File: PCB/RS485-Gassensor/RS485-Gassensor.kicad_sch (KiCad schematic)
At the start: 22 parts, among them J1 Conn_01x04, J2 Conn_01x04, U1 STM8S003F3P, U2 MICS-8614, U3 R-785.0-1.0, U4 LT1785xS8, U5 OP179GRT

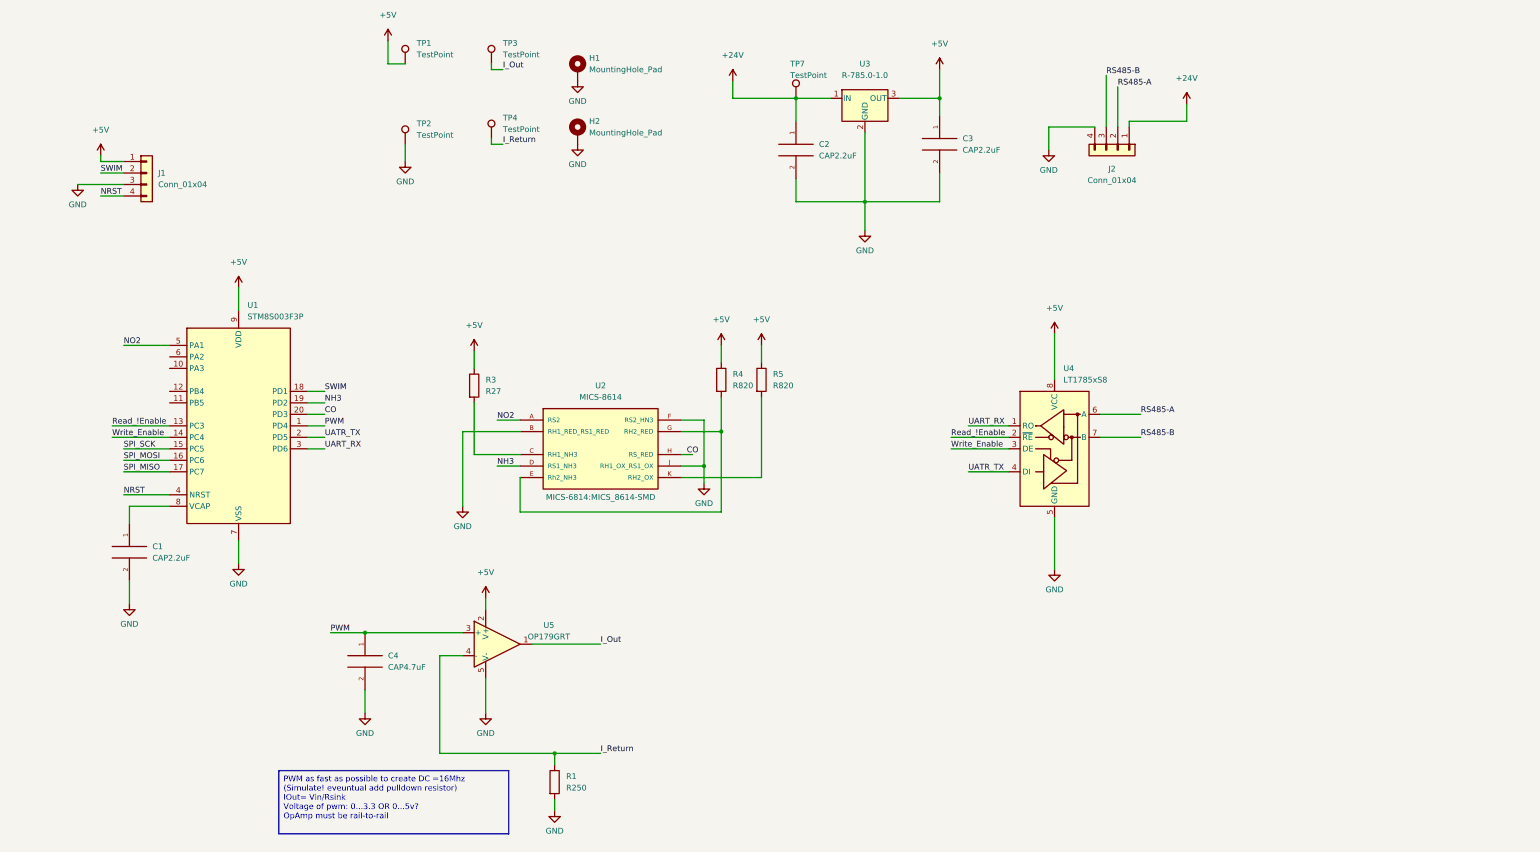
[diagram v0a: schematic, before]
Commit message: clean up, minor extension
cleaned up /reorganized scematic,
added optional termination resistor for RS-485
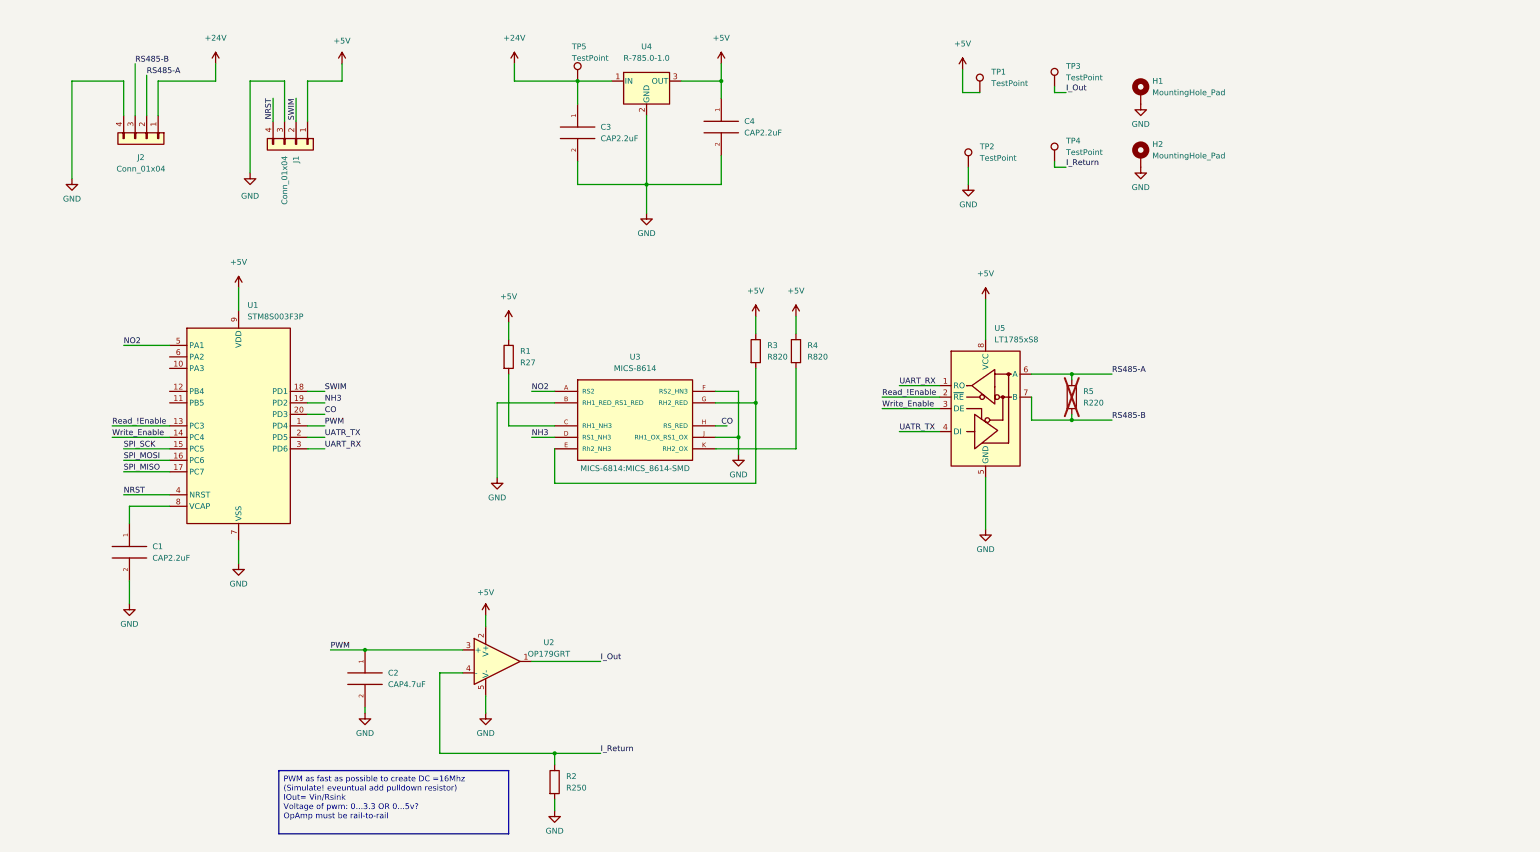
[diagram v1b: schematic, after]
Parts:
- added R5: R220, Capacitor_SMD:C_0603_1608Metric, symbol Device:R
- renumbered C4 to C2, C2 to C3, C3 to C4, R3 to R1, R1 to R2, R4 to R3, R5 to R4, TP7 to TP5, U5 to U2, U2 to U3, U3 to U4, U4 to U5
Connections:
- net RS485-A: now also R5.1
- net RS485-B: now also R5.2
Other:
- moved on the sheet: C2, C3, C4, H1, H2, J1, J2, R1, R3, R4, TP1, TP2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

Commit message: restarted Project.
new PCB, improved component chioce
strarted program with STM32 IDE
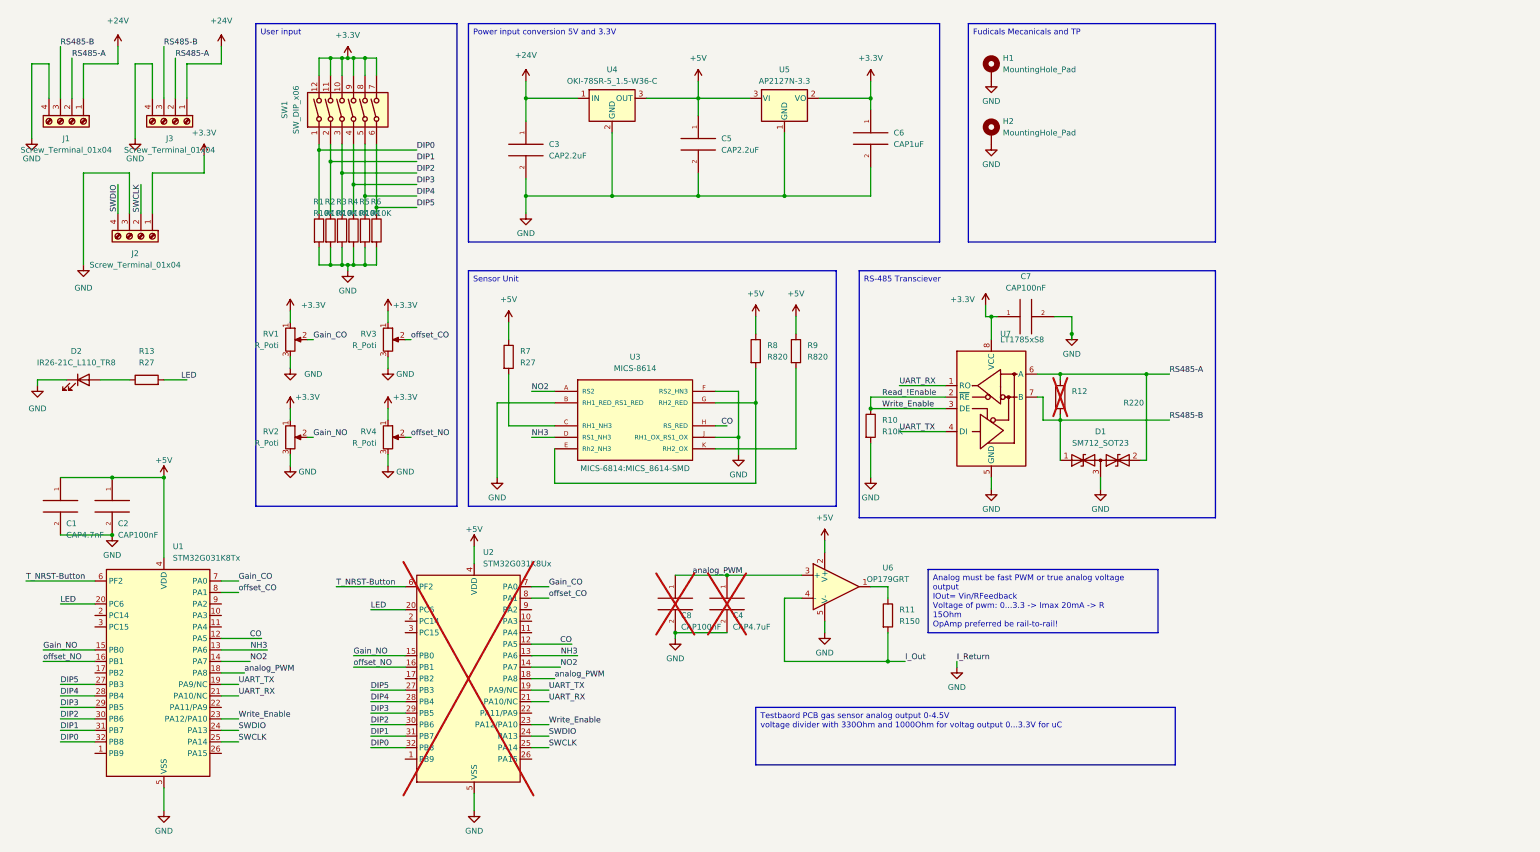
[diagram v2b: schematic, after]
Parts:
- removed J1: Conn_01x04, Connector_PinHeader_2.54mm:PinHeader_1x04_P2.54mm_Vertical, symbol Connector_Generic:Conn_01x04
- removed J2: Conn_01x04, Connector_Phoenix_SPT:PhoenixContact_SPT_1.5_4-H-3.5_1x04_P3.5mm_Horizontal, symbol Connector_Generic:Conn_01x04
- removed TP1, TP2, TP3, TP4, TP5: TestPoint, TestPoint:TestPoint_Pad_D1.0mm, symbol Connector:TestPoint
- removed U1: STM8S003F3P, Package_SO:TSSOP-20_4.4x6.5mm_P0.65mm, symbol MCU_ST_STM8:STM8S003F3P
- removed U4: R-785.0-1.0, Converter_DCDC:Converter_DCDC_RECOM_R-78E-0.5_THT, symbol Regulator_Switching:R-785.0-1.0
- added C2, C7, C8: CAP100nF, Capacitor_SMD:C_0603_1608Metric, symbol pspice:CAP
- added C6: CAP1uF, Capacitor_SMD:C_0603_1608Metric, symbol pspice:CAP
- added D1: SM712_SOT23, Package_TO_SOT_SMD:SOT-23, symbol Diode:SM712_SOT23
- added D2: IR26-21C_L110_TR8, LED_SMD:LED_1206_3216Metric, symbol LED:IR26-21C_L110_TR8
- added J1, J3: Screw_Terminal_01x04, Connector_Phoenix_SPT:PhoenixContact_SPT_1.5_4-H-3.5_1x04_P3.5mm_Horizontal, symbol Connector:Screw_Terminal_01x04
- added J2: Screw_Terminal_01x04, Connector_PinHeader_2.54mm:PinHeader_1x04_P2.54mm_Vertical, symbol Connector:Screw_Terminal_01x04
- added R1, R10, R3, R4, R5, R6: R10K, Capacitor_SMD:C_0603_1608Metric, symbol Device:R
- added R11: R150, Capacitor_SMD:C_1206_3216Metric, symbol Device:R
- added R13: R27, Capacitor_SMD:C_0603_1608Metric, symbol Device:R
- added RV1, RV2, RV3, RV4: R_Poti, PCM_Potentiometer_SMD_AKL:Potentiometer_ACP_CA6-VSMD_Vertical, symbol Device:R_Potentiometer
- added SW1: SW_DIP_x06, Package_DIP:SMDIP-12_W9.53mm, symbol Switch:SW_DIP_x06
- added U1: STM32G031K8Tx, Package_QFP:LQFP-32_7x7mm_P0.8mm, symbol MCU_ST_STM32G0:STM32G031K8Tx
- added U2: STM32G031K8Ux, Package_DFN_QFN:QFN-32-1EP_5x5mm_P0.5mm_EP3.45x3.45mm, symbol MCU_ST_STM32G0:STM32G031K8Ux
- added U4: OKI-78SR-5_1.5-W36-C, Converter_DCDC:Converter_DCDC_Murata_OKI-78SR_Vertical, symbol Converter_DCDC:OKI-78SR-5_1.5-W36-C
- added U5: AP2127N-3.3, Package_TO_SOT_SMD:SOT-23, symbol Regulator_Linear:AP2127N-3.3
- C1: value CAP2.2uF -> CAP4.7nF
- C4: renamed from C2; now not fitted; now left out of the parts list
- R2: value R250 -> R10K
- renumbered C4 to C5, R5 to R12, R1 to R7, R3 to R8, R4 to R9, U2 to U6, U5 to U7
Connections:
- net Write_Enable is gone; now on net Read_!Enable: U7.3 (DE)
- net +24V: now also J1.1 (Pin_1), J3.1 (Pin_1), U4.1 (IN)
- net +5V: now also C1.1, C2.1, U1.4 (VDD), U2.4 (VDD), U4.3 (OUT), U5.3 (VI); no longer U7.8 (VCC)
- net CO: now also U1.12 (PA5), U2.12 (PA5)
- net GND: now also C2.2, C6.2, C7.2, C8.2, D1.3 (common), D2.1 (K), J1.4 (Pin_4), J2.3 (Pin_3), J3.4 (Pin_4), R1.2, R10.2, R3.2, R4.2, R5.2, R6.2, RV1.3, RV2.3, RV3.3, RV4.3, U1.5 (VSS), U2.33 (VSS), U2.5 (VSS), U4.2 (GND), U5.1 (GND)
- net I_Out: now also U6.4 (-), R11.2; no longer U6.1
- net NH3: now also U1.13 (PA6), U2.13 (PA6)
- net NO2: now also U1.14 (PA7), U2.14 (PA7)
- net RS485-A: now also D1.2 (A2), J1.2 (Pin_2), J3.2 (Pin_2)
- net RS485-B: now also D1.1 (A1), J1.3 (Pin_3), J3.3 (Pin_3)
- net Read_!Enable: now also R10.1, U1.23 (PA12/PA10), U2.23 (PA12/PA10)
- net UART_RX: now also U1.21 (PA10/NC), U2.21 (PA10/NC)
- net I_Return renamed DIP1
- net DIP1: now also SW1.2, U1.31 (PB7), U2.31 (PB7); no longer U6.4 (-)
- net PWM renamed analog_PWM
- net analog_PWM: now also C8.1, U1.18 (PA8), U2.18 (PA8)
- net UATR_TX renamed UART_TX
- net UART_TX: now also U1.19 (PA9/NC), U2.19 (PA9/NC)
- new net: R11.1, U6.1
- new net: D2.2 (A), R13.1
- new net +3.3V: C6.1, C7.1, J2.1 (Pin_1), RV1.1, RV2.1, RV3.1, RV4.1, SW1.10, SW1.11, SW1.12, SW1.7, SW1.8, SW1.9, U5.2 (VO), U7.8 (VCC)
- new net DIP0: R1.1, SW1.1, U1.32 (PB8), U2.32 (PB8)
- new net DIP2: R3.1, SW1.3, U1.30 (PB6), U2.30 (PB6)
- new net DIP3: R4.1, SW1.4, U1.29 (PB5), U2.29 (PB5)
- new net DIP4: R5.1, SW1.5, U1.28 (PB4), U2.28 (PB4)
- new net DIP5: R6.1, SW1.6, U1.27 (PB3), U2.27 (PB3)
- new net Gain_CO: RV1.2, U1.7 (PA0), U2.7 (PA0)
- new net Gain_NO: RV2.2, U1.15 (PB0), U2.15 (PB0)
- new net LED: R13.2, U1.20 (PC6), U2.20 (PC6)
- new net SWCLK: J2.2 (Pin_2), U1.25 (PA14), U2.25 (PA14)
- new net SWDIO: J2.4 (Pin_4), U1.24 (PA13), U2.24 (PA13)
- new net T_NRST-Button: U1.6 (PF2), U2.6 (PF2)
- new net offset_CO: RV3.2, U1.8 (PA1), U2.8 (PA1)
- new net offset_NO: RV4.2, U1.16 (PB1), U2.16 (PB1)
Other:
- moved on the sheet: C3, C5, H1, H2, R12, U6, U7

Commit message: new PCB
new PCB, working DMA
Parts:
- removed J3: Screw_Terminal_01x04, Connector_Phoenix_SPT:PhoenixContact_SPT_1.5_4-H-3.5_1x04_P3.5mm_Horizontal, symbol Connector:Screw_Terminal_01x04
- removed U3: MICS-8614, MICS-6814:MICS_8614-SMD, symbol MICS-8614:MICS-8614
- removed U6: OP179GRT, PCM_Package_TO_SOT_SMD_AKL:SOT-23-5, symbol Amplifier_Operational:OP179GRT
- added FD1, FD2: ~, Custom_Library:Alignement_Testpoint_2Layer, symbol Custom:Alignement_Testpoint
- added H3, H4: MountingHole_Pad, MountingHole:MountingHole_3.2mm_M3_DIN965_Pad, symbol Mechanical:MountingHole_Pad
- added J1: Screw_Terminal_01x08, Connector_Phoenix_SPT:1862068, symbol Connector:Screw_Terminal_01x08
- added J4, J5: Screw_Terminal_01x06, Connector_Phoenix_SPT:1071000, symbol Connector:Screw_Terminal_01x06
- added R14, R16, R17, R18, R19: R1K, Capacitor_SMD:C_0603_1608Metric, symbol Device:R
- added R15: R150, Capacitor_SMD:C_1206_3216Metric, symbol Device:R
- added U3, U8: MQ-6, Sensor:MQ-6, symbol Sensor_Gas:MQ-6
- added U6, U9: AD8676xR, Package_SO:SOIC-8_3.9x4.9mm_P1.27mm, symbol Amplifier_Operational:AD8676xR
- C4: value CAP4.7uF -> CAP100nF
- H1, H2: footprint MountingHole:MountingHole_2.2mm_M2_DIN965_Pad -> MountingHole:MountingHole_3.2mm_M3_DIN965_Pad
- J3: renamed from J1; value Screw_Terminal_01x04 -> Screw_Terminal_01x08; footprint Connector_Phoenix_SPT:PhoenixContact_SPT_1.5_4-H-3.5_1x04_P3.5mm_Horizontal -> Connector_Phoenix_SPT:1862068; symbol Connector:Screw_Terminal_01x04 -> Connector:Screw_Terminal_01x08
- R13: value R27 -> R100
- R7: value R27 -> 470R
- R8: value R820 -> R1K
- R9: value R820 -> 470R
- RV1, RV4: value R_Poti -> R_Poti_1K; footprint PCM_Potentiometer_SMD_AKL:Potentiometer_ACP_CA6-VSMD_Vertical -> PCM_Potentiometer_SMD_AKL:Potentiometer_Bourns_3214J_Horizontal
- RV2: renamed from RV3; value R_Poti -> R_Poti_1K; footprint PCM_Potentiometer_SMD_AKL:Potentiometer_ACP_CA6-VSMD_Vertical -> PCM_Potentiometer_SMD_AKL:Potentiometer_Bourns_3214J_Horizontal
- RV3: renamed from RV2; value R_Poti -> R_Poti_1K; footprint PCM_Potentiometer_SMD_AKL:Potentiometer_ACP_CA6-VSMD_Vertical -> PCM_Potentiometer_SMD_AKL:Potentiometer_Bourns_3214J_Horizontal
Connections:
- net NH3 is gone; now on net CO: U1.13 (PA6), U2.13 (PA6)
- net +24V: now also J3.2 (Pin_2), J1.1 (Pin_1), J1.2 (Pin_2), U6.8 (V+), U9.8 (V+)
- net +3.3V: now also C1.1, C2.1, U1.4 (VDD), U2.4 (VDD)
- net +5V: now also U3.2 (VH+), U3.4 (A2), U3.6 (A1), U8.2 (VH+), U8.4 (A2), U8.6 (A1); no longer C1.1, C2.1, R7.1, R8.1, R9.1, U1.4 (VDD), U2.4 (VDD)
- net CO: now also R9.2, R14.2; no longer U1.12 (PA5), U2.12 (PA5)
- net GND: now also J3.7 (Pin_7), J3.8 (Pin_8), R8.1, H3.1, H4.1, J1.7 (Pin_7), J1.8 (Pin_8), J4.3 (Pin_3), J4.4 (Pin_4), J5.3 (Pin_3), J5.4 (Pin_4), R14.1, R18.2, R19.2, U3.5 (VH-), U6.4 (V-), U8.5 (VH-), U9.4 (V-); no longer J3.4 (Pin_4)
- net NO2: now also R7.2, R8.2
- net RS485-A: now also J3.3 (Pin_3), J3.4 (Pin_4), J1.3 (Pin_3), J1.4 (Pin_4); no longer J3.2 (Pin_2)
- net RS485-B: now also J3.5 (Pin_5), J3.6 (Pin_6), J1.5 (Pin_5), J1.6 (Pin_6); no longer J3.3 (Pin_3)
- net at R11.1: now also U9.1
- net I_Out renamed I_Out_CO
- net I_Out_CO: now also J5.5 (Pin_5), J5.6 (Pin_6), U9.2 (-)
- net analog_PWM renamed analog_PWM_CO
- net analog_PWM_CO: now also U9.3 (+), U9.5 (+); no longer C4.1
- new net: R16.1, U9.7
- new net: R17.1, U6.7
- new net: R7.1, U8.1 (B1), U8.3 (B2)
- new net: R15.1, U6.1
- new net: R9.1, U3.1 (B1), U3.3 (B2)
- new net I_Out_NO: J4.5 (Pin_5), J4.6 (Pin_6), R15.2, U6.2 (-)
- new net U_Out_CO: J5.1 (Pin_1), J5.2 (Pin_2), R16.2, R18.1, U9.6 (-)
- new net U_Out_NO: J4.1 (Pin_1), J4.2 (Pin_2), R17.2, R19.1, U6.6 (-)
- new net analog_PWM_NO: C4.1, U1.12 (PA5), U2.12 (PA5), U6.3 (+), U6.5 (+)
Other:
- moved on the sheet: C1, C2, C3, C5, C6, C7, C8, D1, D2, H1, H2, J2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
